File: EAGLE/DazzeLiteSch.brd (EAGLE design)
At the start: 67.2 x 74.7 mm, 21 parts, among them U1 UPDUINO3P0, U2 74AHCT125N

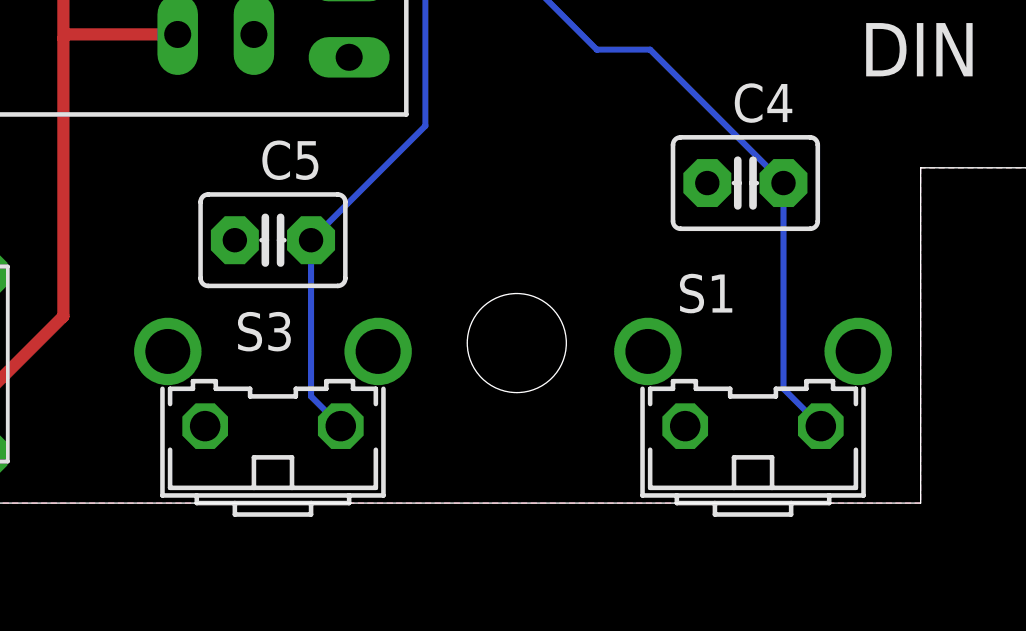
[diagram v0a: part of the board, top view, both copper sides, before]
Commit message: Corrected a few part numbers
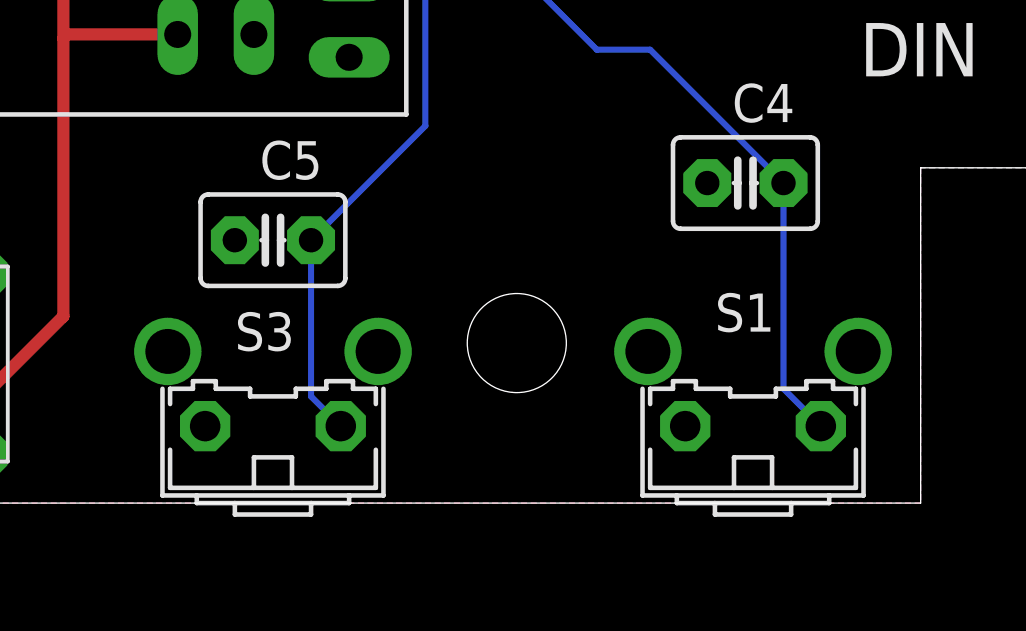
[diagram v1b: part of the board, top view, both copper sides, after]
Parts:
- DC1: value R-78C5.0-1.0 -> TSR_1-2450; device dc-dc-converter:SIP3 -> StarLiteLib:SIP3
- S1, S3: device switch-omron:B3F-31XX -> StarLiteLib:B3F-31XX
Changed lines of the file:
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@@
 <setting verticaltext="up"/>
 </settings>
-<grid distance="0.025" unitdist="inch" unit="inch" style="dots" multiple="1" display="yes" altdistance="0.01" altunitdist="inch" altunit="inch"/>
+<grid distance="0.025" unitdist="inch" unit="inch" style="dots" multiple="1" display="yes" altdistance="0.005" altunitdist="inch" altunit="inch"/>
 <layers>
 <layer number="1" name="Top" color="4" fill="1" visible="yes" active="yes"/>
@@
 <attribute name="VALUE" x="59.309" y="13.208" size="1.27" layer="27" ratio="10" rot="R180"/>
 </element>
-<element name="DC1" library="dc-dc-converter" library_urn="urn:adsk.eagle:library:208" package="SIP3" package3d_urn="urn:adsk.eagle:package:12318/1" value="R-78C5.0-1.0" x="10.033" y="36.322" smashed="yes" rot="R90">
+<element name="DC1" library="StarLiteLib" package="SIP3" package3d_urn="urn:adsk.eagle:package:12318/1" value="TSR_1-2450" x="10.033" y="36.322" smashed="yes" rot="R90">
 <attribute name="NAME" x="2.667" y="34.671" size="1.27" layer="25" rot="R90"/>
-<attribute name="POPULARITY" value="0" x="10.033" y="36.322" size="1.778" layer="27" rot="R90" display="off"/>
+<attribute name="POPULARITY" value="" x="10.033" y="36.322" size="1.778" layer="27" rot="R90" display="off"/>
 <attribute name="VALUE" x="7.493" y="31.242" size="1.27" layer="27" rot="R90"/>
 </element>
@@
 <attribute name="VALUE" x="13.462" y="48.006" size="1.27" layer="27" ratio="10" rot="R180"/>
 </element>
-<element name="S1" library="switch-omron" library_urn="urn:adsk.eagle:library:377" package="B3F-31XX" package3d_urn="urn:adsk.eagle:package:27487/1" value="1-1825027-1" x="57.912" y="3.302" smashed="yes">
-<attribute name="MF" value="" x="57.912" y="3.302" size="1.778" layer="27" display="off"/>
-<attribute name="MPN" value="B3F-3100" x="57.912" y="3.302" size="1.778" layer="27" display="off"/>
-<attribute name="NAME" x="55.372" y="5.842" size="1.27" layer="25" ratio="10"/>
-<attribute name="OC_FARNELL" value="959704" x="57.912" y="3.302" size="1.778" layer="27" display="off"/>
-<attribute name="OC_NEWARK" value="36M3582" x="57.912" y="3.302" size="1.778" layer="27" display="off"/>
-<attribute name="POPULARITY" value="0" x="57.912" y="3.302" size="1.778" layer="27" display="off"/>
-<attribute name="VALUE" x="54.229" y="-2.667" size="1.27" layer="27" ratio="10"/>
-</element>
 <element name="U1" library="StarLiteLib" package="UPDUINO3P0" value="UPDUINO3P0" x="36.83" y="38.481" smashed="yes" rot="R90">
 <attribute name="NAME" x="23.114" y="72.009" size="1.778" layer="25" ratio="10" rot="R180"/>
@@
 <attribute name="POPULARITY" value="38" x="41.91" y="8.255" size="1.778" layer="27" rot="R180" display="off"/>
 <attribute name="VALUE" x="43.561" y="11.303" size="1.27" layer="27" ratio="10" rot="R180"/>
-</element>
-<element name="S3" library="switch-omron" library_urn="urn:adsk.eagle:library:377" package="B3F-31XX" package3d_urn="urn:adsk.eagle:package:27487/1" value="1-1825027-1" x="41.91" y="3.302" smashed="yes">
-<attribute name="MF" value="" x="41.91" y="3.302" size="1.778" layer="27" display="off"/>
-<attribute name="MPN" value="B3F-3100" x="41.91" y="3.302" size="1.778" layer="27" display="off"/>
-<attribute name="NAME" x="40.64" y="4.572" size="1.27" layer="25" ratio="10"/>
-<attribute name="OC_FARNELL" value="959704" x="41.91" y="3.302" size="1.778" layer="27" display="off"/>
-<attribute name="OC_NEWARK" value="36M3582" x="41.91" y="3.302" size="1.778" layer="27" display="off"/>
-<attribute name="POPULARITY" value="0" x="41.91" y="3.302" size="1.778" layer="27" display="off"/>
-<attribute name="VALUE" x="38.227" y="-2.667" size="1.27" layer="27" ratio="10"/>
 </element>
 <element name="S2" library="StarLiteLib" package="DPDT157" value="EG2219" x="26.162" y="4.1275" smashed="yes" rot="R180">
@@
 <attribute name="SPICEPREFIX" value="R" x="10.16" y="11.43" size="1.778" layer="27" rot="R180" display="off"/>
 <attribute name="VALUE" x="11.7856" y="11.9126" size="0.9906" layer="27" ratio="10" rot="R180"/>
+</element>
+<element name="S3" library="StarLiteLib" package="B3F-31XX" package3d_urn="urn:adsk.eagle:package:27487/1" value="1-1825027-1" x="41.91" y="3.302" smashed="yes">
+<attribute name="DIGIKEY" value="450-1658-ND" x="41.91" y="3.302" size="1.778" layer="27" display="off"/>
+<attribute name="MF" value="" x="41.91" y="3.302" size="1.778" layer="27" display="off"/>
+<attribute name="MPN" value="1-1825027-1" x="41.91" y="3.302" size="1.778" layer="27" display="off"/>
+<attribute name="NAME" x="40.64" y="4.572" size="1.27" layer="25" ratio="10"/>
+<attribute name="POPULARITY" value="0" x="41.91" y="3.302" size="1.778" layer="27" display="off"/>
+<attribute name="VALUE" x="38.227" y="-2.667" size="1.27" layer="27" ratio="10"/>
+</element>
+<element name="S1" library="StarLiteLib" package="B3F-31XX" package3d_urn="urn:adsk.eagle:package:27487/1" value="1-1825027-1" x="57.912" y="3.302" smashed="yes">
+<attribute name="DIGIKEY" value="450-1658-ND" x="57.912" y="3.302" size="1.778" layer="27" display="off"/>
+<attribute name="MF" value="" x="57.912" y="3.302" size="1.778" layer="27" display="off"/>
+<attribute name="MPN" value="1-1825027-1" x="57.912" y="3.302" size="1.778" layer="27" display="off"/>
+<attribute name="NAME" x="56.642" y="5.207" size="1.27" layer="25" ratio="10"/>
+<attribute name="POPULARITY" value="0" x="57.912" y="3.302" size="1.778" layer="27" display="off"/>
+<attribute name="VALUE" x="54.229" y="-2.667" size="1.27" layer="27" ratio="10"/>
 </element>
 </elements>
@@
 <contactref element="C3" pad="2"/>
 <contactref element="C5" pad="2"/>
-<contactref element="S3" pad="1"/>
 <contactref element="C4" pad="2"/>
-<contactref element="S1" pad="1"/>
 <contactref element="TP7" pad="TP"/>
 <contactref element="TP2" pad="TP"/>
@@
 <contactref element="U1" pad="GND3"/>
 <contactref element="U1" pad="GND4"/>
+<contactref element="S3" pad="1"/>
+<contactref element="S1" pad="1"/>
 </signal>
 <signal name="VCC">
@@
 <signal name="DISP_SEL_N">
 <contactref element="C4" pad="1"/>
-<contactref element="S1" pad="2"/>
-<wire x1="58.928" y1="10.16" x2="58.928" y2="3.302" width="0.2032" layer="16"/>
-<wire x1="58.928" y1="3.302" x2="60.1726" y2="2.0574" width="0.2032" layer="16"/>
+<wire x1="58.928" y1="3.302" x2="58.928" y2="10.16" width="0.2032" layer="16"/>
 <wire x1="58.928" y1="10.16" x2="54.483" y2="14.605" width="0.2032" layer="16"/>
 <wire x1="52.705" y1="14.605" x2="54.483" y2="14.605" width="0.2032" layer="16"/>
@@
 <wire x1="48.895" y1="38.1" x2="48.895" y2="18.415" width="0.2032" layer="16"/>
 <wire x1="48.895" y1="18.415" x2="52.705" y2="14.605" width="0.2032" layer="16"/>
+<contactref element="S1" pad="2"/>
+<wire x1="60.1726" y1="2.0574" x2="58.928" y2="3.302" width="0.2032" layer="16"/>
 </signal>
 <signal name="BRITE_SEL_N">
 <contactref element="C5" pad="1"/>
-<contactref element="S3" pad="2"/>
-<wire x1="44.1706" y1="2.0574" x2="43.18" y2="3.048" width="0.2032" layer="16"/>
 <wire x1="43.18" y1="3.048" x2="43.18" y2="8.255" width="0.2032" layer="16"/>
 <contactref element="U1" pad="9"/>
@@
 <wire x1="45.974" y1="37.211" x2="44.45" y2="37.211" width="0.2032" layer="16"/>
 <wire x1="46.99" y1="36.195" x2="45.974" y2="37.211" width="0.2032" layer="16"/>
+<contactref element="S3" pad="2"/>
+<wire x1="44.1706" y1="2.0574" x2="43.18" y2="3.048" width="0.2032" layer="16"/>
 </signal>
 <signal name="BATT_SW">
